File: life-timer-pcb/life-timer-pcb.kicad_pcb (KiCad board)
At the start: 2 copper layers, 39 x 30.8 mm, 20 parts, among them J1 SSD1306_Socket, SW1 SW_RST, SW2 SW_Push, SW3 SW_Push, SW4 SW_Push, SW5 SW_PWR, U1 ATtiny85-20S

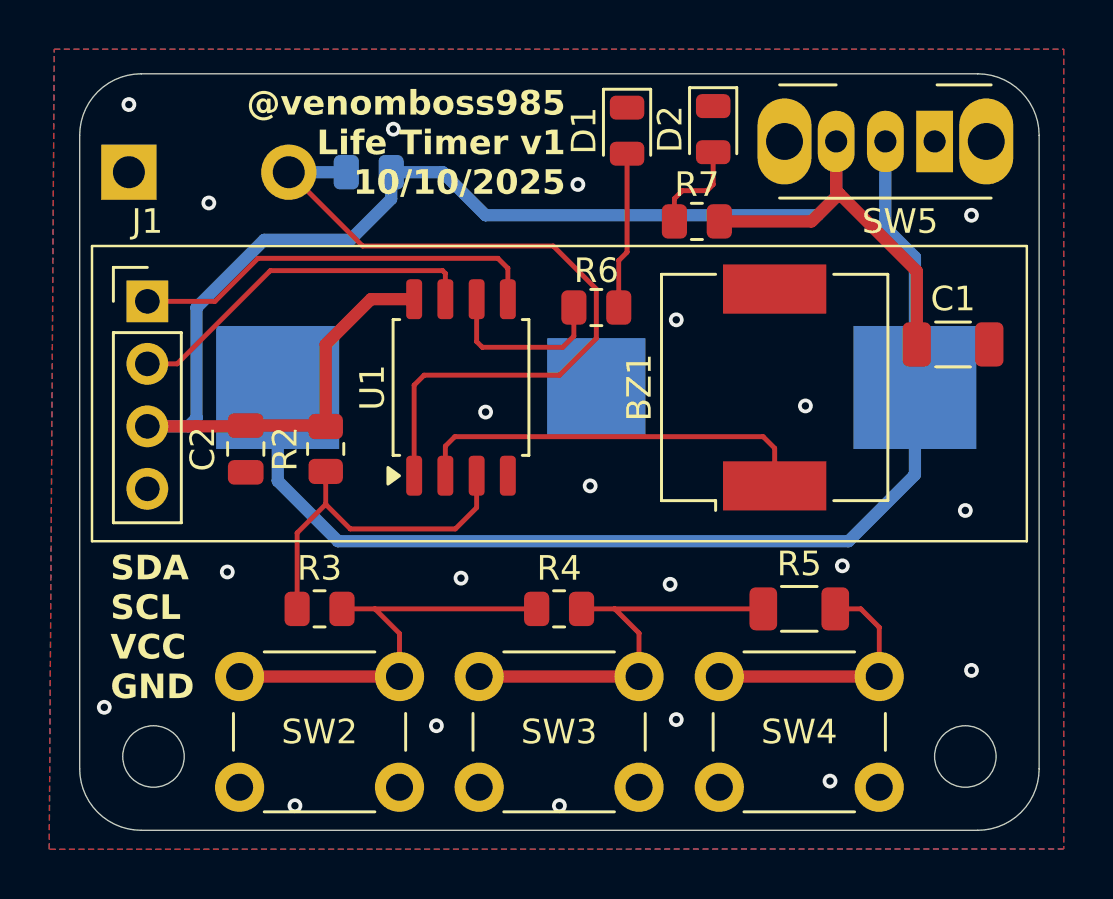
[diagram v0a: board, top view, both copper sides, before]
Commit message: Added reset line to OLED socket; passes ERC/DRC
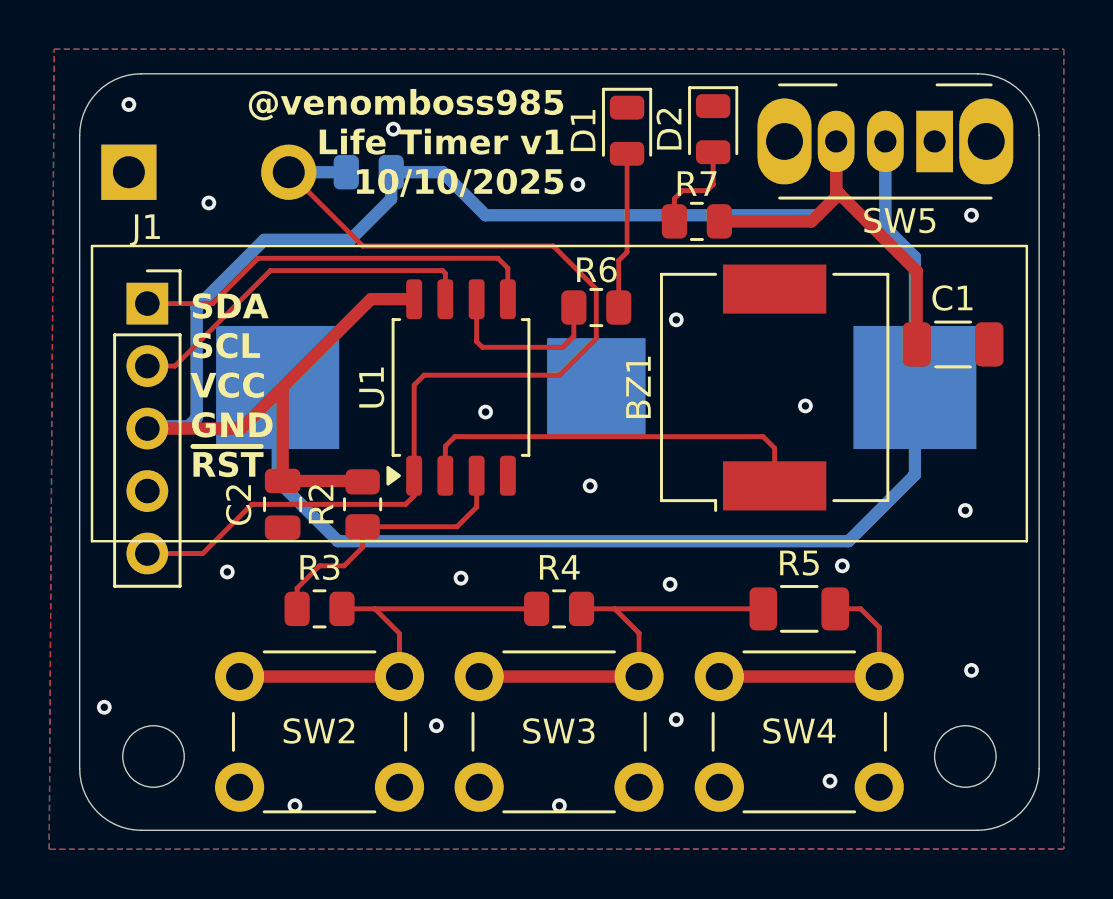
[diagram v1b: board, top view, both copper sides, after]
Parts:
- J1: footprint Connector_PinHeader_2.54mm:PinHeader_1x04_P2.54mm_Vertical -> Connector_PinSocket_2.54mm:PinSocket_1x05_P2.54mm_Vertical
- moved C2 2.70 mm to (135.2, 103.5)
- moved R2 2.70 mm to (138.5, 103.5)
- moved J1 0.09 mm to (129.8, 95.3)
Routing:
- net ~{RESET}: track 30.7 -> 43.3 mm
- net VCC: track 68.8 -> 73.9 mm
- net BTNS: track 14.3 -> 11.3 mm
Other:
- board text added: "SDA SCL VCC GND ~{RST}"
- board text removed: "SDA SCL VCC GND"
